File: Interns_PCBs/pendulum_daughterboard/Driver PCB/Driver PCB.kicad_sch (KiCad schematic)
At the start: 6 parts, among them J5 DRIVE_GND, J7 DRIVE_5V_IN

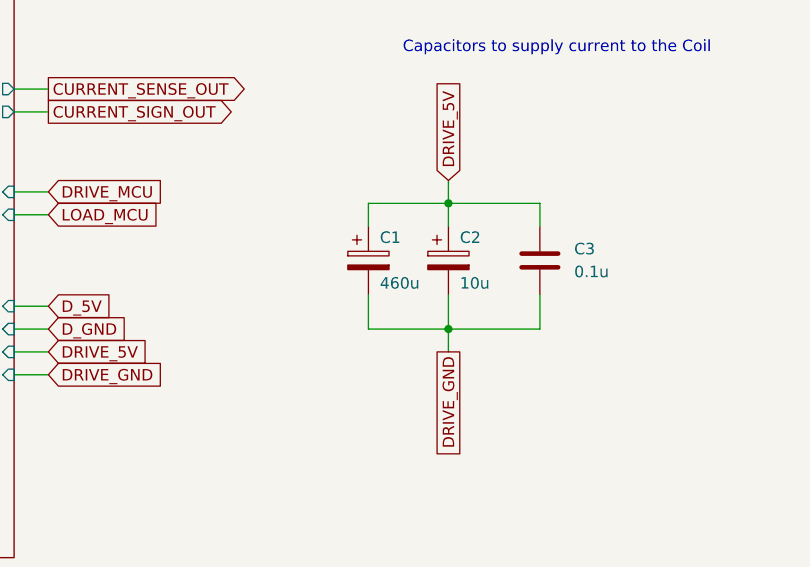
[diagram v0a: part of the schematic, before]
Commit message: Changes with the Components
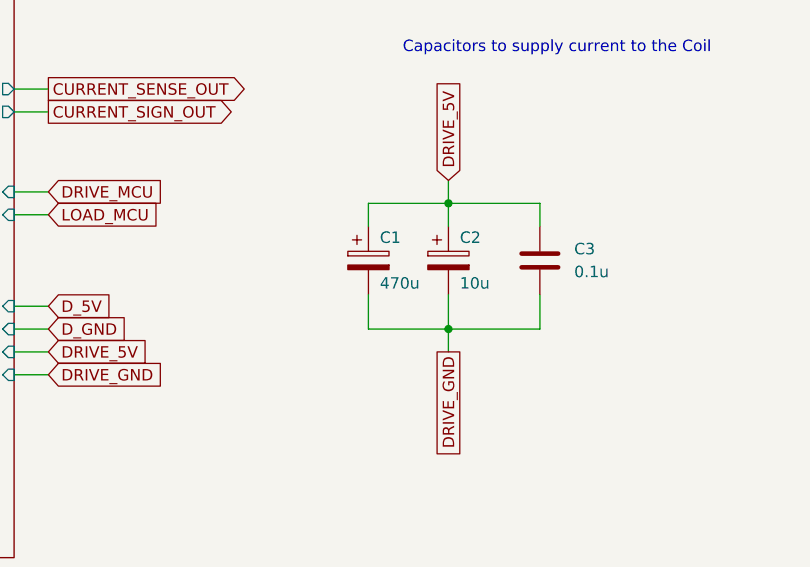
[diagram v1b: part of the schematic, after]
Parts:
- C1: value 460u -> 470u; footprint Capacitor_SMD:C_0805_2012Metric_Pad1.18x1.45mm_HandSolder -> Capacitor_SMD:C_Elec_8x10.2
- C2: footprint Capacitor_SMD:C_0805_2012Metric_Pad1.18x1.45mm_HandSolder -> Capacitor_SMD:CP_Elec_3x5.3
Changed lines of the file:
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@@
       (effects (font (size 1.27 1.27)) (justify left))
     )
-    (property "Footprint" "Capacitor_SMD:C_0805_2012Metric_Pad1.18x1.45mm_HandSolder" (id 2) (at 144.4752 151.13 0)
+    (property "Footprint" "Capacitor_SMD:CP_Elec_3x5.3" (id 2) (at 144.4752 151.13 0)
       (effects (font (size 1.27 1.27)) hide)
     )
@@
       (effects (font (size 1.27 1.27)) (justify left))
     )
-    (property "Value" "460u" (id 1) (at 135.89 149.86 0)
-      (effects (font (size 1.27 1.27)) (justify left))
-    )
-    (property "Footprint" "Capacitor_SMD:C_0805_2012Metric_Pad1.18x1.45mm_HandSolder" (id 2) (at 135.5852 151.13 0)
+    (property "Value" "470u" (id 1) (at 135.89 149.86 0)
+      (effects (font (size 1.27 1.27)) (justify left))
+    )
+    (property "Footprint" "Capacitor_SMD:C_Elec_8x10.2" (id 2) (at 135.5852 151.13 0)
       (effects (font (size 1.27 1.27)) hide)
     )
@@
     )
     (path "/6e693a78-a1bf-4a7f-8c1f-510085fc4108"
-      (reference "C1") (unit 1) (value "460u") (footprint "Capacitor_SMD:C_0805_2012Metric_Pad1.18x1.45mm_HandSolder")
+      (reference "C1") (unit 1) (value "470u") (footprint "Capacitor_SMD:C_Elec_8x10.2")
     )
     (path "/3c70c001-d248-412e-93f6-0eb0062cefbc"
-      (reference "C2") (unit 1) (value "10u") (footprint "Capacitor_SMD:C_0805_2012Metric_Pad1.18x1.45mm_HandSolder")
+      (reference "C2") (unit 1) (value "10u") (footprint "Capacitor_SMD:CP_Elec_3x5.3")
     )
     (path "/85f35f61-4dfb-4f91-a35e-e378a90c4aa8"

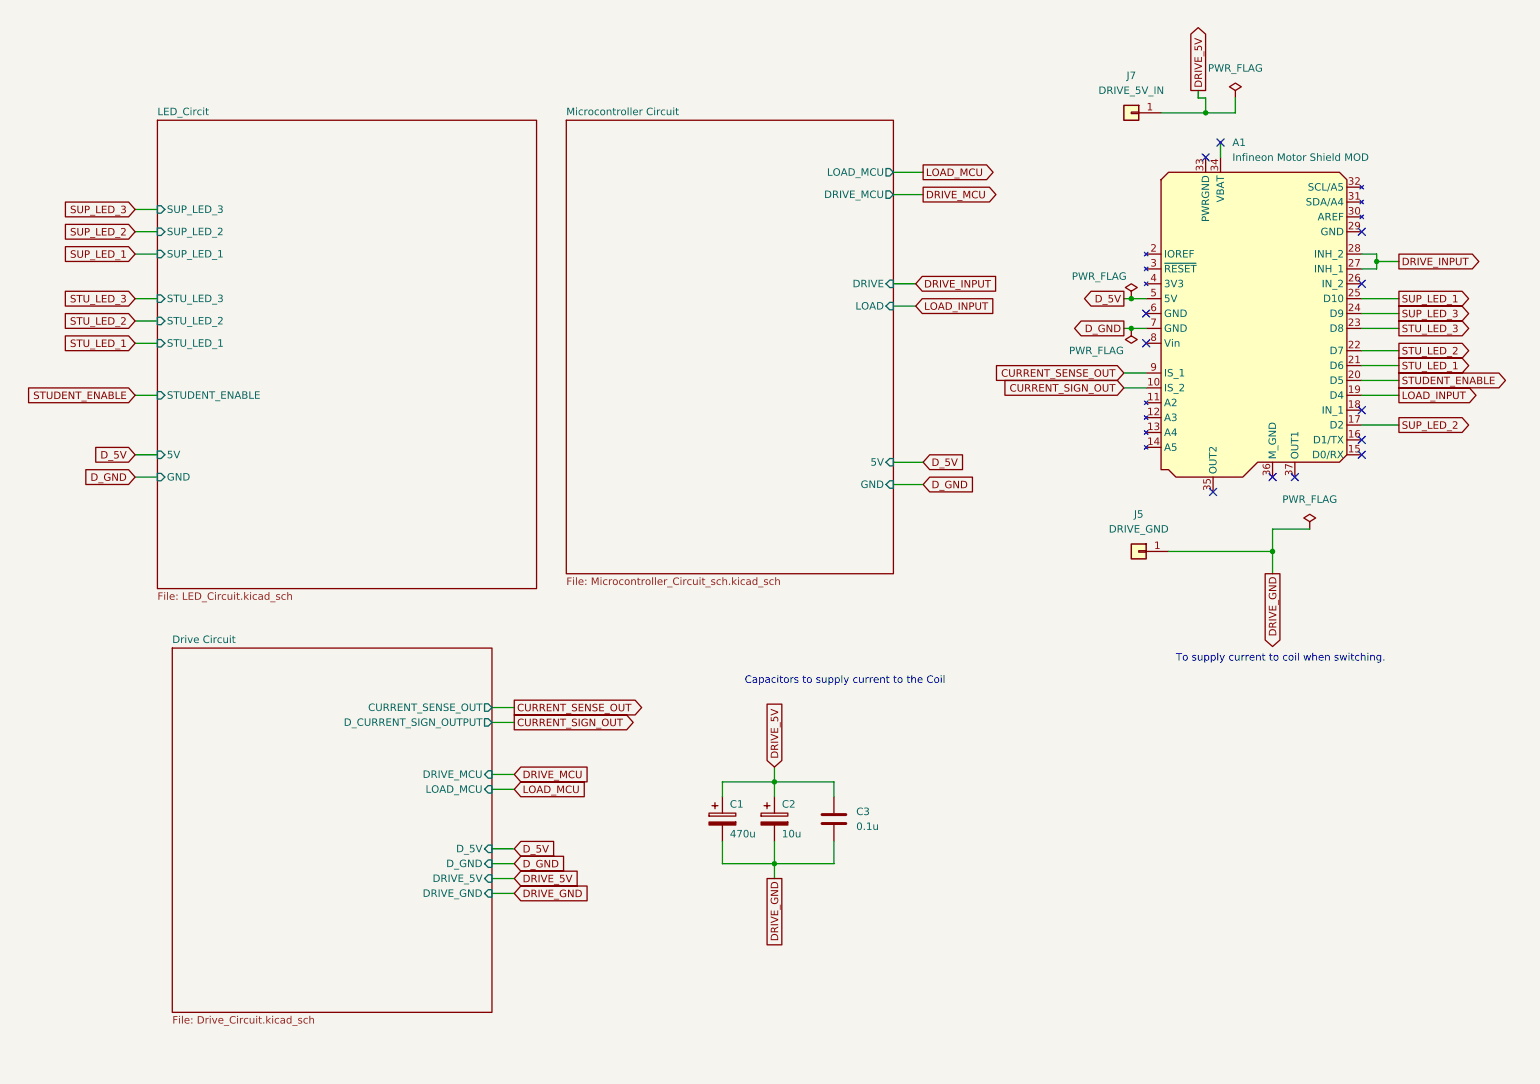
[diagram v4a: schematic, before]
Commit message: Pull down and Current Limiting Resistors
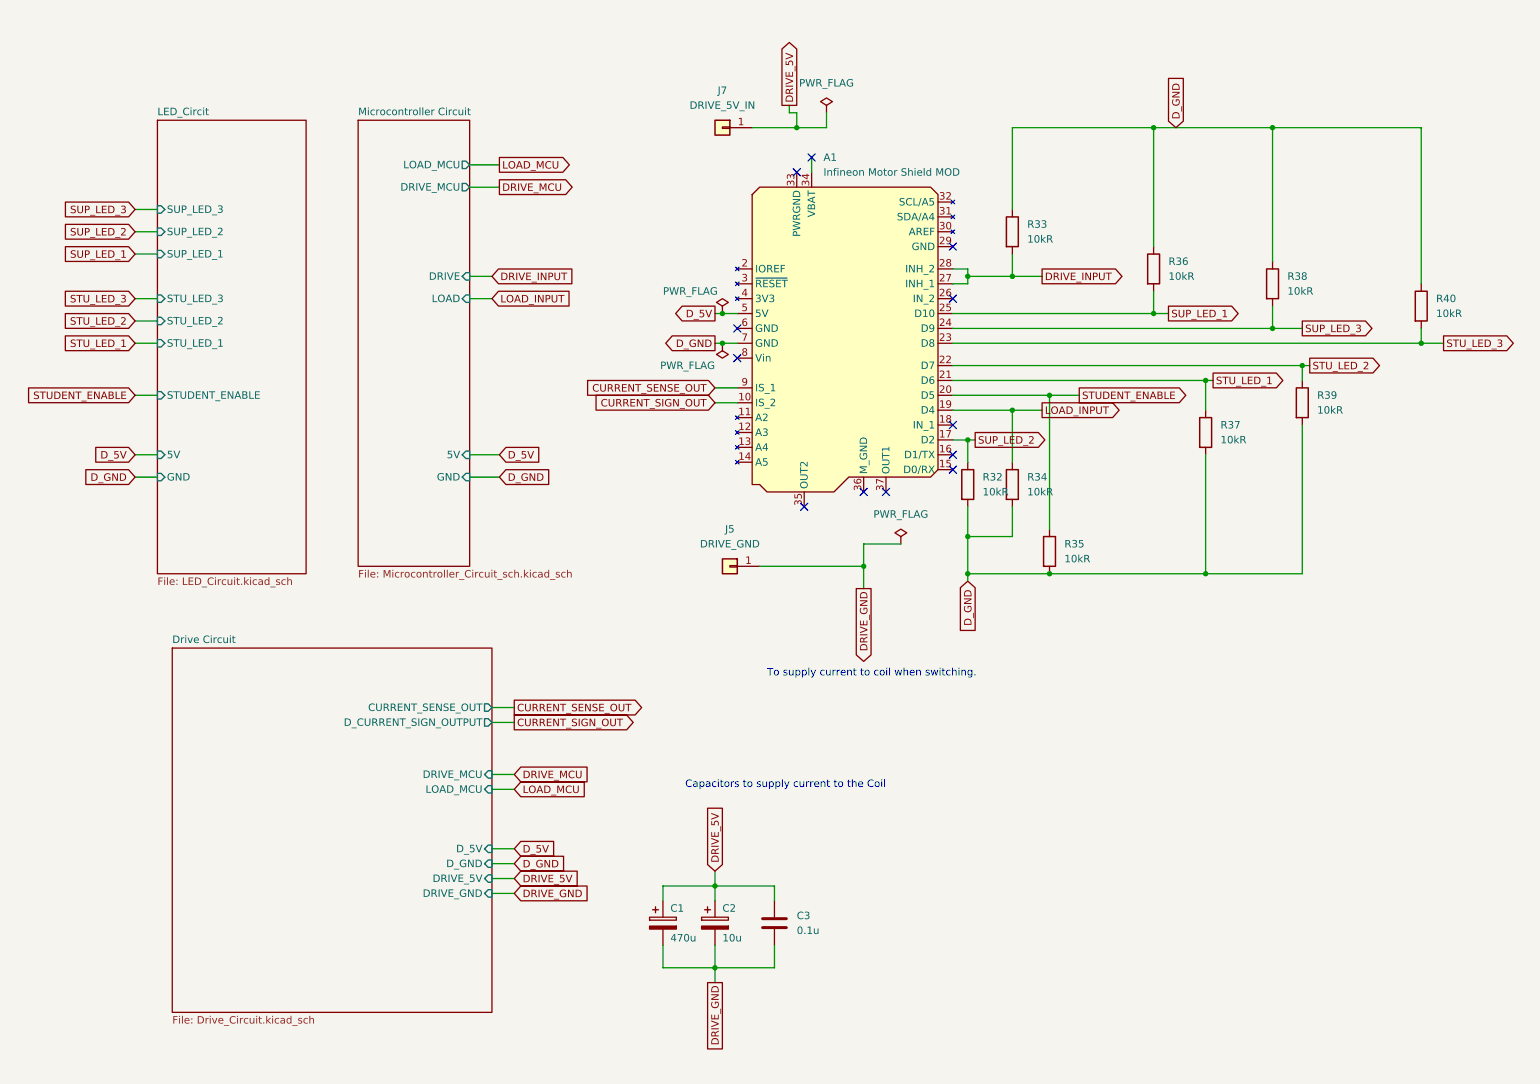
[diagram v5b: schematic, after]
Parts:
- added R32, R33, R34, R35, R36, R37, R38, R39, R40: 10kR, symbol Device:R
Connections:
- net DRIVE_INPUT: now also R33.2
- net D_GND: now also R32.2, R33.1, R34.2, R35.2, R36.1, R37.2, R38.1, R39.2, R40.1
- net LOAD_INPUT: now also R34.1
- net STUDENT_ENABLE: now also R35.1
- net STU_LED_1: now also R37.1
- net STU_LED_2: now also R39.1
- net STU_LED_3: now also R40.2
- net SUP_LED_1: now also R36.2
- net SUP_LED_2: now also R32.1
- net SUP_LED_3: now also R38.2
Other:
- moved on the sheet: A1, C1, C2, C3, J5, J7
